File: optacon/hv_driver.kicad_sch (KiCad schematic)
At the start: 11 parts

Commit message: driver board
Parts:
- added R6: 0, Resistor_SMD:R_0603_1608Metric, symbol Device:R
- C1: value (none) -> 1 µF; footprint (none) -> Capacitor_SMD:C_0603_1608Metric
- C2, C3: value (none) -> 0.1 µF; footprint (none) -> Capacitor_SMD:C_0603_1608Metric
- C4: value (none) -> 0.1 µF 150V+; footprint (none) -> Capacitor_SMD:C_1206_3216Metric
- L1: value (none) -> VLS3012HBX-3R3M; footprint (none) -> microchip_hv:TDK_VLS_3012; Part TDK VLS 3012 -> (none)
- R1: value (none) -> 549k; footprint (none) -> Resistor_SMD:R_0603_1608Metric
- R2, R3: value (none) -> 6.98k; footprint (none) -> Resistor_SMD:R_0603_1608Metric
- R4, R5: value (none) -> 3.3k; footprint (none) -> Resistor_SMD:R_0603_1608Metric
- U3: value (none) -> DRV2665; footprint (none) -> Package_DFN_QFN:Texas_S-PVQFN-N20_EP2.7x2.7mm_ThermalVias
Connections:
- net REG: now also R6.1; no longer C3.1, U3.20 (REG)
- net VBST: now reaches C4.1, R1.1, U3.10 (VBST), U3.11 (VBST), U3.12 (PVDD)
- new net: C3.1, R6.2, U3.20 (REG)
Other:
- note removed: "Q: add 0ohm resistors to select VBST instead of OUT+ as output?"
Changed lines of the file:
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@@
   (junction (at 72.39 99.06) (diameter 0) (color 0 0 0 0)
   )
+  (junction (at 151.13 64.77) (diameter 0) (color 0 0 0 0)
+  )
   (junction (at 139.7 83.82) (diameter 0) (color 0 0 0 0)
   )
@@
     (stroke (width 0) (type default) (color 0 0 0 0))
   )
+  (wire (pts (xy 66.04 99.06) (xy 72.39 99.06))
+    (stroke (width 0) (type default) (color 0 0 0 0))
+  )
   (wire (pts (xy 139.7 83.82) (xy 139.7 82.55))
     (stroke (width 0) (type default) (color 0 0 0 0))
   )
-  (polyline (pts (xy 151.13 102.87) (xy 151.13 97.79))
-    (stroke (width 0) (type default) (color 0 0 0 0))
-  )
   (wire (pts (xy 59.69 93.98) (xy 104.14 93.98))
     (stroke (width 0) (type default) (color 0 0 0 0))
@@
     (stroke (width 0) (type default) (color 0 0 0 0))
   )
-  (polyline (pts (xy 152.4 97.79) (xy 218.44 97.79))
-    (stroke (width 0) (type default) (color 0 0 0 0))
-  )
   (wire (pts (xy 104.14 88.9) (xy 92.71 88.9))
     (stroke (width 0) (type default) (color 0 0 0 0))
@@
     (stroke (width 0) (type default) (color 0 0 0 0))
   )
+  (wire (pts (xy 151.13 64.77) (xy 180.34 64.77))
+    (stroke (width 0) (type default) (color 0 0 0 0))
+  )
   (wire (pts (xy 147.32 91.44) (xy 147.32 95.25))
     (stroke (width 0) (type default) (color 0 0 0 0))
@@
     (stroke (width 0) (type default) (color 0 0 0 0))
   )
-  (polyline (pts (xy 218.44 102.87) (xy 151.13 102.87))
-    (stroke (width 0) (type default) (color 0 0 0 0))
-  )
   (wire (pts (xy 127 64.77) (xy 139.7 64.77))
     (stroke (width 0) (type default) (color 0 0 0 0))
   )
-  (wire (pts (xy 54.61 99.06) (xy 72.39 99.06))
+  (wire (pts (xy 54.61 99.06) (xy 58.42 99.06))
     (stroke (width 0) (type default) (color 0 0 0 0))
   )
@@
     (stroke (width 0) (type default) (color 0 0 0 0))
   )
-  (polyline (pts (xy 218.44 97.79) (xy 218.44 102.87))
-    (stroke (width 0) (type default) (color 0 0 0 0))
-  )
   (wire (pts (xy 134.62 91.44) (xy 137.16 91.44))
     (stroke (width 0) (type default) (color 0 0 0 0))
@@
     (stroke (width 0) (type default) (color 0 0 0 0))
   )
-  (polyline (pts (xy 151.13 97.79) (xy 158.75 97.79))
-    (stroke (width 0) (type default) (color 0 0 0 0))
-  )
   (wire (pts (xy 134.62 76.2) (xy 139.7 76.2))
     (stroke (width 0) (type default) (color 0 0 0 0))
@@
   (wire (pts (xy 119.38 44.45) (xy 119.38 53.34))
     (stroke (width 0) (type default) (color 0 0 0 0))
-  )
-  (text "Q: add 0ohm resistors to select VBST instead of OUT+ as output?"
-    (at 152.4 101.6 0)
-    (effects (font (size 1.27 1.27)) (justify left bottom))
   )
   (hierarchical_label "SDA" (shape bidirectional) (at 54.61 96.52 180)
@@
     (effects (font (size 1.27 1.27)) (justify right))
   )
+  (hierarchical_label "VBST" (shape input) (at 180.34 64.77 0)
+    (effects (font (size 1.27 1.27)) (justify left))
+  )
   (hierarchical_label "VDD" (shape input) (at 54.61 44.45 180)
     (effects (font (size 1.27 1.27)) (justify right))
@@
       (effects (font (size 1.27 1.27)) (justify left))
     )
-    (property "Value" "" (id 1) (at 83.82 78.7399 0)
-      (effects (font (size 1.27 1.27)) (justify left))
-    )
-    (property "Footprint" "" (id 2) (at 80.9752 81.28 0)
+    (property "Value" "0.1 µF" (id 1) (at 83.82 78.7399 0)
+      (effects (font (size 1.27 1.27)) (justify left))
+    )
+    (property "Footprint" "Capacitor_SMD:C_0603_1608Metric" (id 2) (at 80.9752 81.28 0)
       (effects (font (size 1.27 1.27)) hide)
     )
@@
     )
     (property "Part" "C30926" (id 4) (at 80.01 77.47 0)
+      (effects (font (size 1.27 1.27)) hide)
+    )
+    (pin "1")
+    (pin "2")
+  )
+  (symbol (lib_id "Device:R") (at 62.23 99.06 90) (unit 1)
+    (in_bom yes) (on_board yes)
+    (property "Reference" "R6" (id 0) (at 62.23 101.6 90))
+    (property "Value" "0" (id 1) (at 62.23 104.14 90))
+    (property "Footprint" "Resistor_SMD:R_0603_1608Metric" (id 2) (at 62.23 100.838 90)
+      (effects (font (size 1.27 1.27)) hide)
+    )
+    (property "Datasheet" "~" (id 3) (at 62.23 99.06 0)
       (effects (font (size 1.27 1.27)) hide)
     )
@@
       (effects (font (size 1.27 1.27)) (justify left))
     )
-    (property "Value" "" (id 1) (at 154.94 69.8499 0)
-      (effects (font (size 1.27 1.27)) (justify left))
-    )
-    (property "Footprint" "" (id 2) (at 152.0952 72.39 0)
+    (property "Value" "0.1 µF 150V+" (id 1) (at 154.94 69.8499 0)
+      (effects (font (size 1.27 1.27)) (justify left))
+    )
+    (property "Footprint" "Capacitor_SMD:C_1206_3216Metric" (id 2) (at 152.0952 72.39 0)
       (effects (font (size 1.27 1.27)) (justify left))
     )
@@
       (effects (font (size 1.27 1.27)) (justify left))
     )
-    (property "Value" "" (id 1) (at 142.24 73.66 0)
-      (effects (font (size 1.27 1.27)) (justify left))
-    )
-    (property "Footprint" "" (id 2) (at 137.922 72.39 90)
+    (property "Value" "549k" (id 1) (at 142.24 73.66 0)
+      (effects (font (size 1.27 1.27)) (justify left))
+    )
+    (property "Footprint" "Resistor_SMD:R_0603_1608Metric" (id 2) (at 137.922 72.39 90)
       (effects (font (size 1.27 1.27)) hide)
     )
@@
       (effects (font (size 1.27 1.27)) (justify left))
     )
-    (property "Value" "" (id 1) (at 107.95 58.4199 0)
-      (effects (font (size 1.27 1.27)) (justify left))
-    )
-    (property "Footprint" "" (id 2) (at 105.1052 60.96 0)
+    (property "Value" "1 µF" (id 1) (at 107.95 58.4199 0)
+      (effects (font (size 1.27 1.27)) (justify left))
+    )
+    (property "Footprint" "Capacitor_SMD:C_0603_1608Metric" (id 2) (at 105.1052 60.96 0)
       (effects (font (size 1.27 1.27)) hide)
     )
@@
       (effects (font (size 1.27 1.27)) (justify left))
     )
-    (property "Value" "" (id 1) (at 99.06 77.4699 0)
-      (effects (font (size 1.27 1.27)) (justify left))
-    )
-    (property "Footprint" "" (id 2) (at 97.79 76.2 0)
+    (property "Value" " VLS3012HBX-3R3M" (id 1) (at 99.06 77.4699 0)
+      (effects (font (size 1.27 1.27)) (justify left))
+    )
+    (property "Footprint" "microchip_hv:TDK_VLS_3012" (id 2) (at 97.79 76.2 0)
       (effects (font (size 1.27 1.27)) hide)
     )
@@
       (effects (font (size 1.27 1.27)) hide)
     )
-    (property "Part" "TDK VLS 3012" (id 4) (at 97.79 76.2 0)
+    (property "Part" " " (id 4) (at 97.79 76.2 0)
       (effects (font (size 1.27 1.27)) hide)
     )
@@
       (effects (font (size 1.27 1.27)) (justify left))
     )
-    (property "Value" "" (id 1) (at 76.2 104.1399 0)
-      (effects (font (size 1.27 1.27)) (justify left))
-    )
-    (property "Footprint" "" (id 2) (at 73.3552 106.68 0)
+    (property "Value" "0.1 µF" (id 1) (at 76.2 104.1399 0)
+      (effects (font (size 1.27 1.27)) (justify left))
+    )
+    (property "Footprint" "Capacitor_SMD:C_0603_1608Metric" (id 2) (at 73.3552 106.68 0)
       (effects (font (size 1.27 1.27)) hide)
     )
@@
       (effects (font (size 1.27 1.27)) (justify right))
     )
-    (property "Value" "" (id 1) (at 62.23 90.1699 0)
+    (property "Value" "3.3k" (id 1) (at 62.23 90.1699 0)
       (effects (font (size 1.27 1.27)) (justify right))
     )
-    (property "Footprint" "" (id 2) (at 61.468 88.9 90)
+    (property "Footprint" "Resistor_SMD:R_0603_1608Metric" (id 2) (at 61.468 88.9 90)
       (effects (font (size 1.27 1.27)) hide)
     )
@@
     (in_bom yes) (on_board yes)
     (property "Reference" "R2" (id 0) (at 143.51 78.74 0))
-    (property "Value" "" (id 1) (at 144.78 81.28 0))
-    (property "Footprint" "" (id 2) (at 141.478 80.01 90)
+    (property "Value" "6.98k" (id 1) (at 144.78 81.28 0))
+    (property "Footprint" "Resistor_SMD:R_0603_1608Metric" (id 2) (at 141.478 80.01 90)
       (effects (font (size 1.27 1.27)) hide)
     )
@@
     (in_bom yes) (on_board yes)
     (property "Reference" "R3" (id 0) (at 140.97 93.98 90))
-    (property "Value" "" (id 1) (at 140.97 96.52 90))
-    (property "Footprint" "" (id 2) (at 140.97 93.218 90)
+    (property "Value" "6.98k" (id 1) (at 140.97 96.52 90))
+    (property "Footprint" "Resistor_SMD:R_0603_1608Metric" (id 2) (at 140.97 93.218 90)
       (effects (font (size 1.27 1.27)) hide)
     )
@@
       (effects (font (size 1.27 1.27)) (justify left))
     )
-    (property "Value" "" (id 1) (at 72.39 90.1699 0)
-      (effects (font (size 1.27 1.27)) (justify left))
-    )
-    (property "Footprint" "" (id 2) (at 68.072 88.9 90)
+    (property "Value" "3.3k" (id 1) (at 72.39 90.1699 0)
+      (effects (font (size 1.27 1.27)) (justify left))
+    )
+    (property "Footprint" "Resistor_SMD:R_0603_1608Metric" (id 2) (at 68.072 88.9 90)
       (effects (font (size 1.27 1.27)) hide)
     )
@@
       (effects (font (size 1.27 1.27)) (justify left))
     )
-    (property "Value" "" (id 1) (at 121.3994 121.92 0)
-      (effects (font (size 1.27 1.27)) (justify left))
-    )
-    (property "Footprint" "" (id 2) (at 120.65 118.11 0)
+    (property "Value" "DRV2665" (id 1) (at 121.3994 121.92 0)
+      (effects (font (size 1.27 1.27)) (justify left))
+    )
+    (property "Footprint" "Package_DFN_QFN:Texas_S-PVQFN-N20_EP2.7x2.7mm_ThermalVias" (id 2) (at 120.65 118.11 0)
       (effects (font (size 1.27 1.27)) (justify left) hide)
     )

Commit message: gerbers
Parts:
- L1: Part (none) -> VLS3012HBX-3R3M
- R6: value 0 -> DNP
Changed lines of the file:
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@@
     (in_bom yes) (on_board yes)
     (property "Reference" "R6" (id 0) (at 62.23 101.6 90))
-    (property "Value" "0" (id 1) (at 62.23 104.14 90))
+    (property "Value" "DNP" (id 1) (at 62.23 104.14 90))
     (property "Footprint" "Resistor_SMD:R_0603_1608Metric" (id 2) (at 62.23 100.838 90)
       (effects (font (size 1.27 1.27)) hide)
@@
       (effects (font (size 1.27 1.27)) hide)
     )
-    (property "Part" " " (id 4) (at 97.79 76.2 0)
+    (property "Part" "VLS3012HBX-3R3M" (id 4) (at 97.79 76.2 0)
       (effects (font (size 1.27 1.27)) hide)
     )

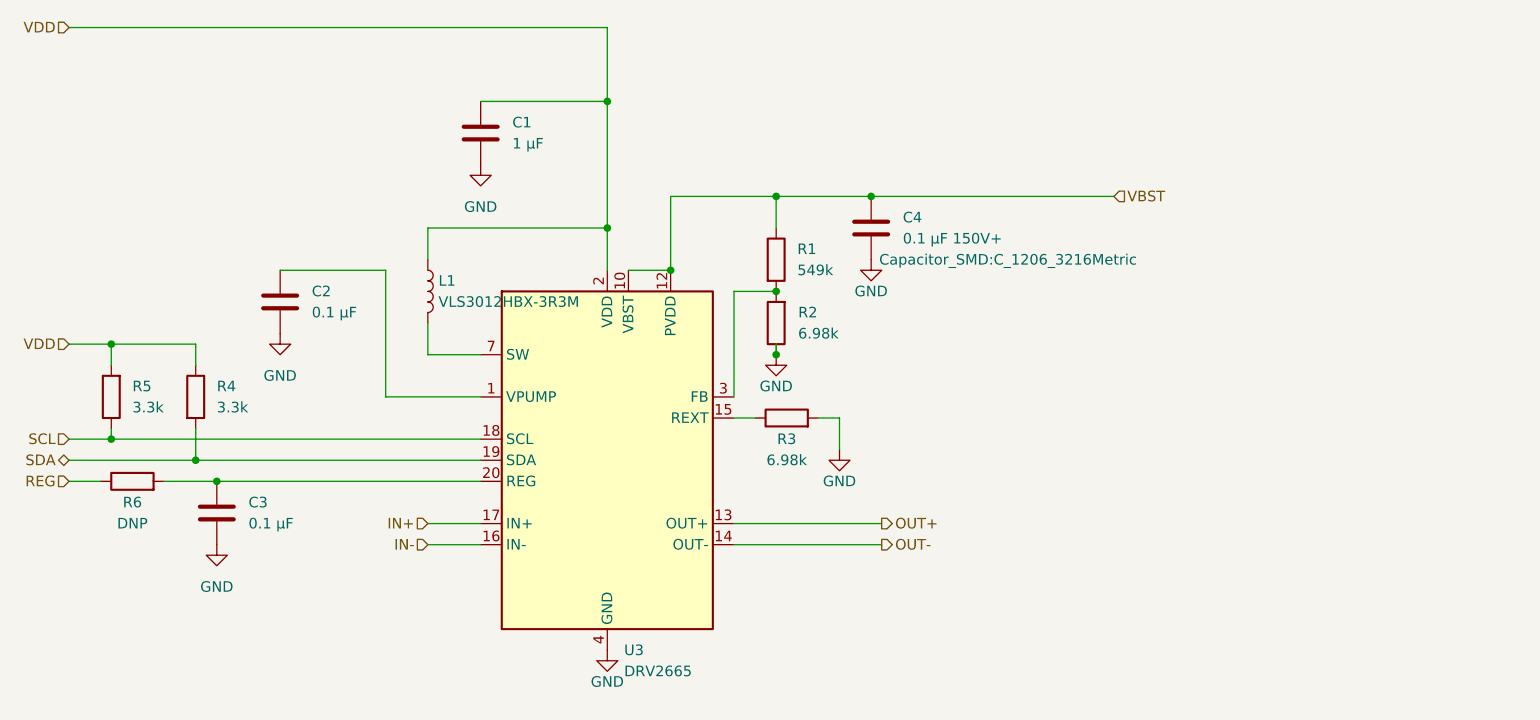
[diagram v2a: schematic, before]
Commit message: WIP -added clearance for reeds center conductor header pins -removed jumper resistor & output cap on VBST -changed C4 high voltage cap to 0805, lower height above board -added C5 10µF cap at inductor -changed hole pattern on piezo to PTH for smaller holes -added copper fill under piezo for equal height -removed alignment holes around piezo, replaced with front silkscreen alignment arrows -reworked layout on DRV2665 a bit according to datasheet guidelines -moved fpc connector to top
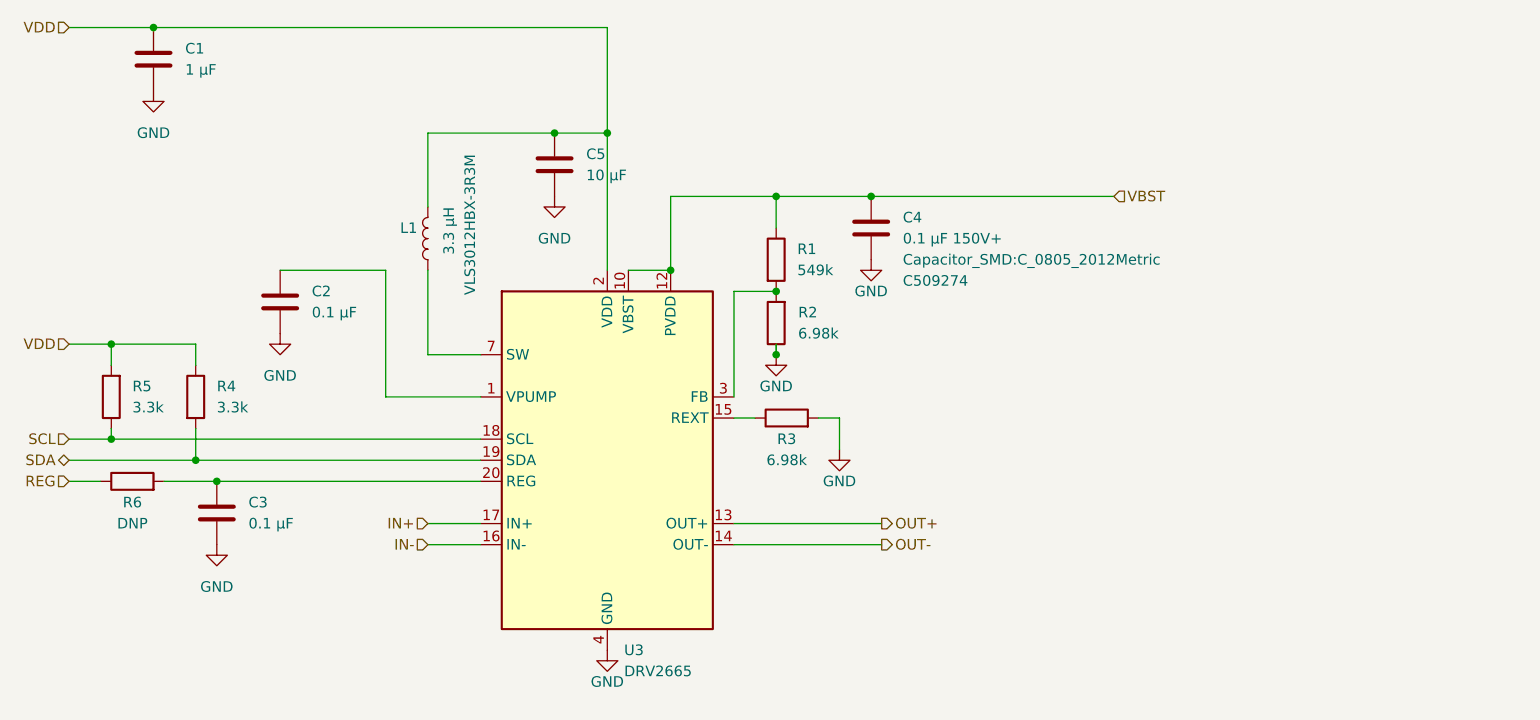
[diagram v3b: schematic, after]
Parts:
- added C5: 10 µF, Capacitor_SMD:C_0603_1608Metric, symbol Device:C
- C4: footprint Capacitor_SMD:C_1206_3216Metric -> Capacitor_SMD:C_0805_2012Metric; Part C76671 -> C509274
- L1: value VLS3012HBX-3R3M -> 3.3 µH
- R6: now left out of the parts list
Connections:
- net GND: now also C5.2
- net VDD: now also L1.2, C5.1; no longer L1.1
- net at U3.7 (SW), U3.8 (SW): now also L1.1; no longer L1.2
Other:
- moved on the sheet: C1, L1

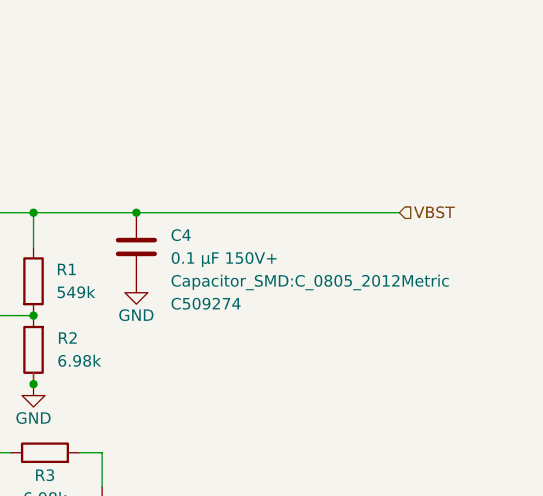
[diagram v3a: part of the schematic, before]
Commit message: hierarchical sheet for shift registers
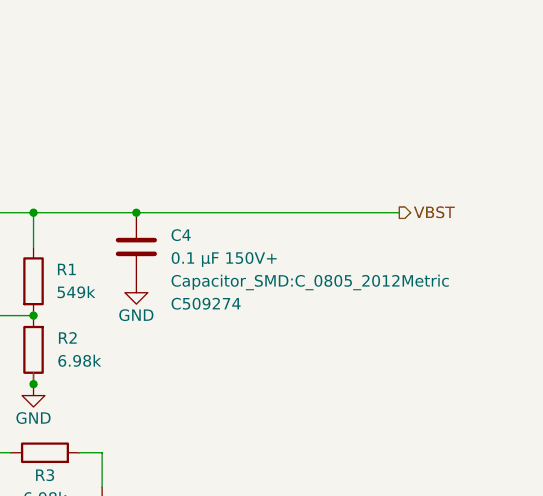
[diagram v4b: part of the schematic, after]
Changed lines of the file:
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@@
     (effects (font (size 1.27 1.27)) (justify right))
   )
-  (hierarchical_label "VBST" (shape input) (at 180.34 64.77 0)
+  (hierarchical_label "VBST" (shape output) (at 180.34 64.77 0)
     (effects (font (size 1.27 1.27)) (justify left))
   )

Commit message: pcb + stencils ordered from pcbgogo
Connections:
- net EN: now reaches C3.1, R6.2, U3.20 (REG)
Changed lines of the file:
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@@
   (junction (at 119.38 57.15) (diameter 0) (color 0 0 0 0)
+  )
+  (junction (at 68.58 99.06) (diameter 0) (color 0 0 0 0)
   )
   (junction (at 127 73.66) (diameter 0) (color 0 0 0 0)
@@
     (stroke (width 0) (type default) (color 0 0 0 0))
   )
-  (wire (pts (xy 66.04 99.06) (xy 72.39 99.06))
+  (wire (pts (xy 66.04 99.06) (xy 68.58 99.06))
     (stroke (width 0) (type default) (color 0 0 0 0))
   )
@@
   )
   (wire (pts (xy 97.79 73.66) (xy 97.79 83.82))
+    (stroke (width 0) (type default) (color 0 0 0 0))
+  )
+  (wire (pts (xy 68.58 99.06) (xy 68.58 106.68))
     (stroke (width 0) (type default) (color 0 0 0 0))
   )
@@
     (stroke (width 0) (type default) (color 0 0 0 0))
   )
+  (wire (pts (xy 68.58 99.06) (xy 72.39 99.06))
+    (stroke (width 0) (type default) (color 0 0 0 0))
+  )
   (wire (pts (xy 54.61 99.06) (xy 58.42 99.06))
     (stroke (width 0) (type default) (color 0 0 0 0))
@@
   )
   (wire (pts (xy 97.79 83.82) (xy 104.14 83.82))
+    (stroke (width 0) (type default) (color 0 0 0 0))
+  )
+  (wire (pts (xy 54.61 106.68) (xy 68.58 106.68))
     (stroke (width 0) (type default) (color 0 0 0 0))
   )
@@
     (effects (font (size 1.27 1.27)) (justify left))
   )
+  (hierarchical_label "EN" (shape input) (at 54.61 106.68 180)
+    (effects (font (size 1.27 1.27)) (justify right))
+  )
   (hierarchical_label "VDD" (shape input) (at 54.61 82.55 180)

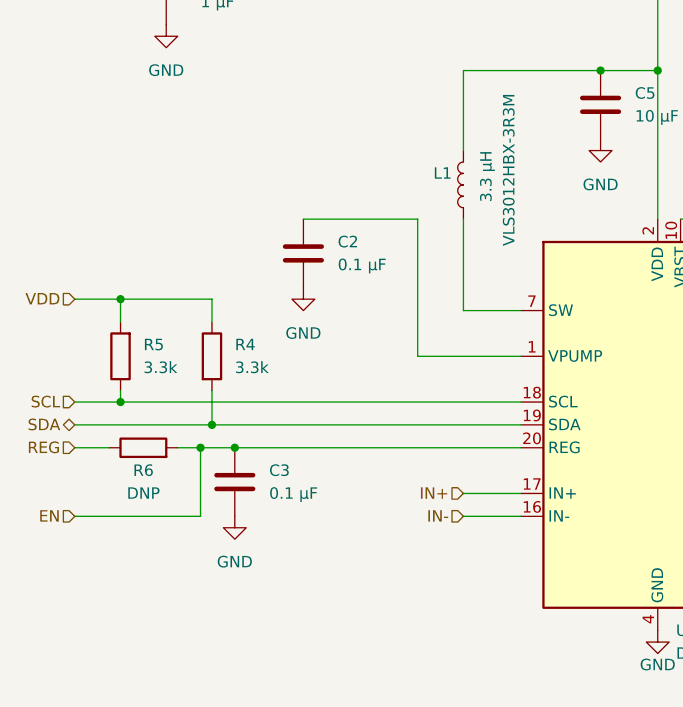
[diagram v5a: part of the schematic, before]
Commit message: remove VBIAS, EN, REG rename & reorder nets for i2c, spi add IN- next to IN+ (AIN) add SMD FPC connector for piezo use BP instead of HVOUTs for piezo_common
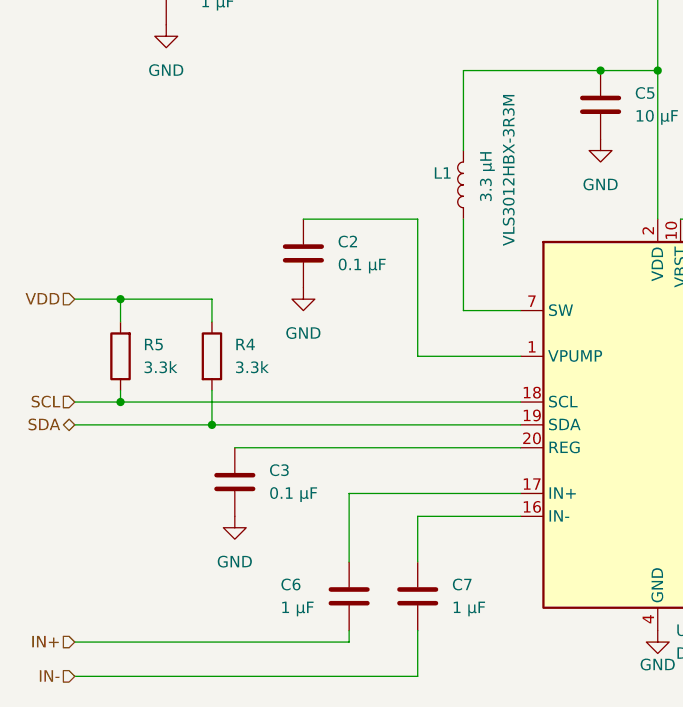
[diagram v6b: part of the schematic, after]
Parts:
- removed R6: DNP, Resistor_SMD:R_0603_1608Metric, symbol Device:R
- added C6, C7: 1 µF, Capacitor_SMD:C_0603_1608Metric, symbol Device:C
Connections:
- net IN+: now also C6.2; no longer U3.17 (IN+)
- net IN-: now also C7.2; no longer U3.16 (IN-)
- net EN: no longer names the net of C3.1, U3.20 (REG)
- new net: C6.1, U3.17 (IN+)
- new net: C7.1, U3.16 (IN-)

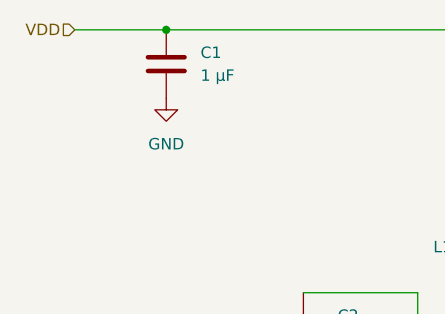
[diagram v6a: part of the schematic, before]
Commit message: separate VIN and VDD
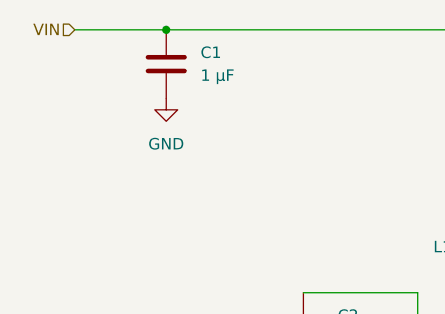
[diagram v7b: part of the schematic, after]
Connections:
- net VDD: no longer C1.1, C5.1, L1.2, U3.2 (VDD)
- new net VIN: C1.1, C5.1, L1.2, U3.2 (VDD)
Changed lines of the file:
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@@
     (effects (font (size 1.27 1.27)) (justify left))
   )
-  (hierarchical_label "VDD" (shape input) (at 54.61 44.45 180) (fields_autoplaced)
+  (hierarchical_label "VIN" (shape input) (at 54.61 44.45 180) (fields_autoplaced)
     (effects (font (size 1.27 1.27)) (justify right))
   )
